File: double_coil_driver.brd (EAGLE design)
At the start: 50 x 50 mm, 62 parts, among them Q1 MOSFET-N, Q3 IRF7493, U1 MCP6L01UT-E/OT, U2 V_REG_LDOSMD, U3 LT3750EMSPBF, X2 MICROMATCH-10

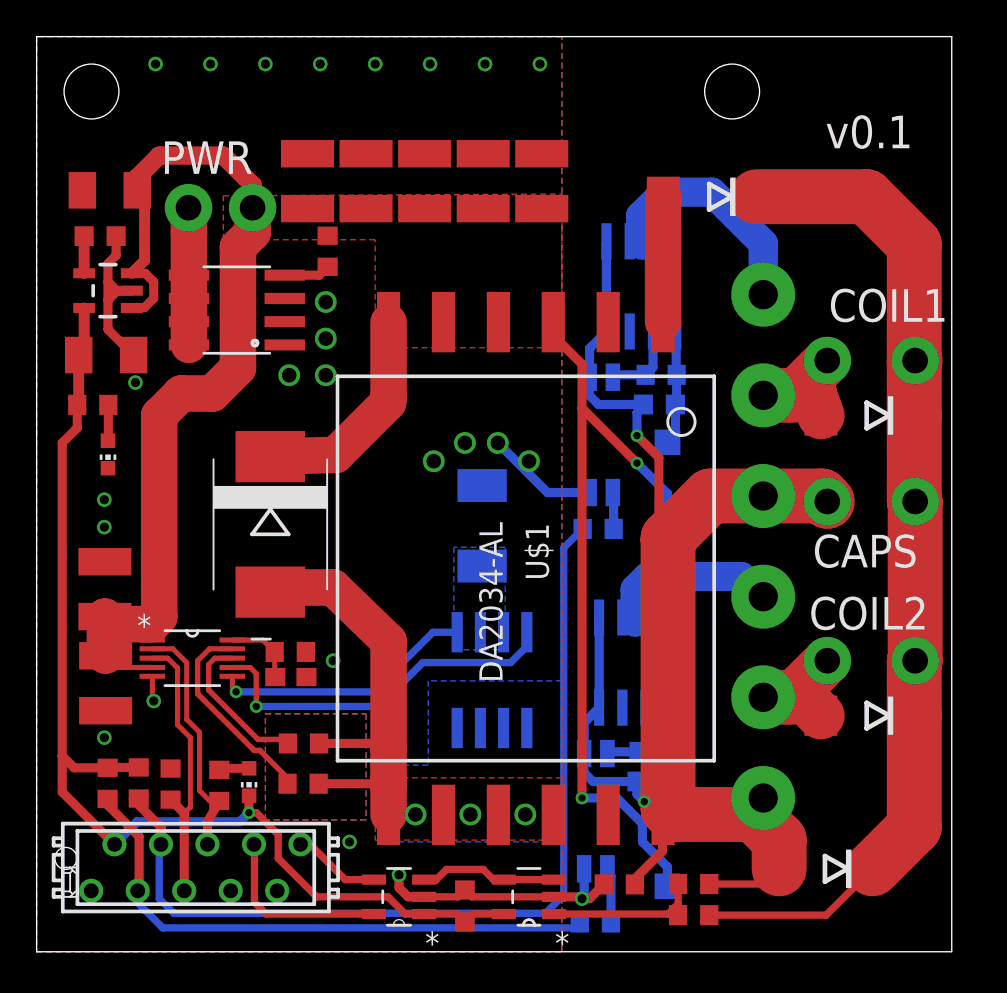
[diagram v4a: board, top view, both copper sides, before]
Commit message: Changed kick pull-ups to pull-downs
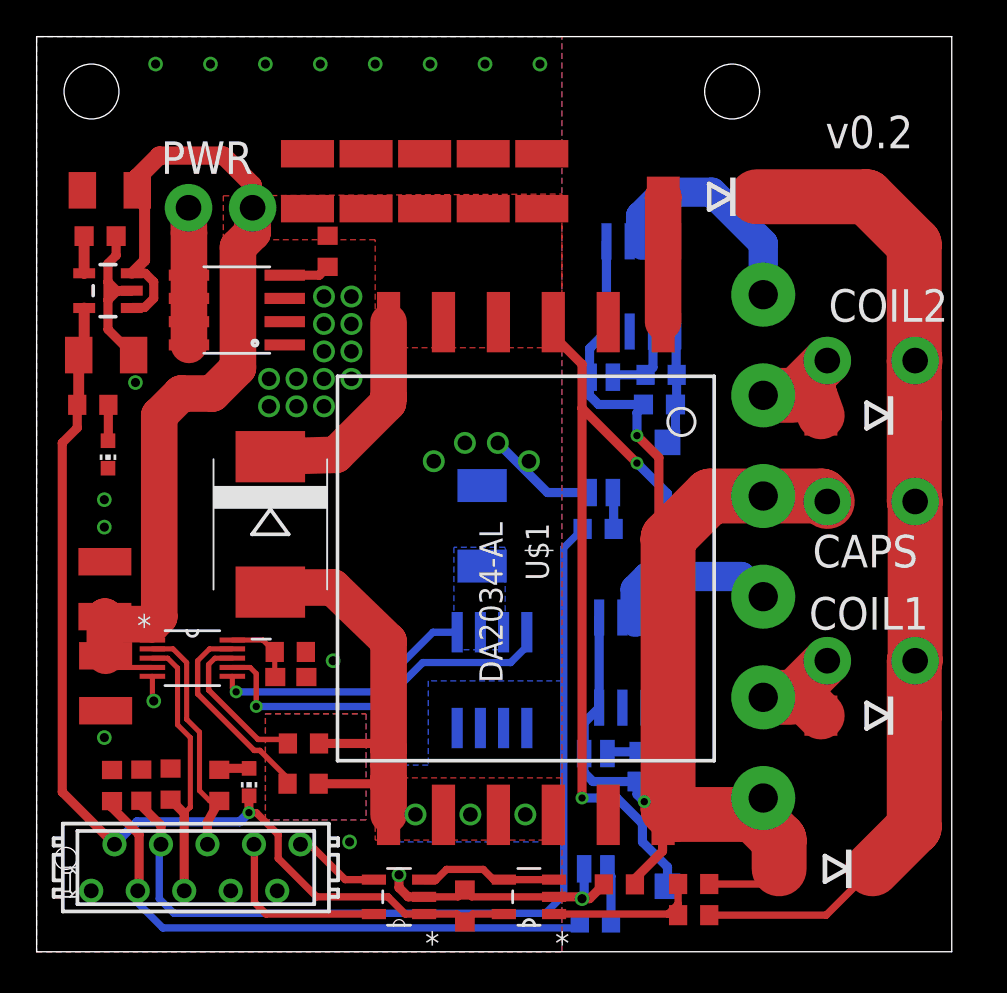
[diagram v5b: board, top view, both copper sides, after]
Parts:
- moved R15 1.84 mm to (5.72, 9.10), turned to 270 degrees
- moved R16 1.47 mm to (4.12, 9.08), turned to 270 degrees
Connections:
- net +5V: no longer R15.2, R16.2
- net GNDA: now also R15.1, R16.1
- net KICK1: now also R16.2; no longer R15.1
- net KICK2: now also R15.2; no longer R16.1
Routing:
- net +5V: track 61.9 -> 57.5 mm
- net KICK2: track 49.7 -> 49.1 mm
- net GNDA: vias 25 -> 34
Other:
- board text added: "v0.2"
- board text removed: "v0.1"
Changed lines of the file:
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@@
 <?xml version="1.0" encoding="utf-8"?>
 <!DOCTYPE eagle SYSTEM "eagle.dtd">
-<eagle version="6.5.0">
+<eagle version="7.0.0">
 <drawing>
 <settings>
@@
 <hole x="3" y="47" drill="3"/>
 <hole x="38" y="47" drill="3"/>
-<text x="49.8" y="36.2" size="1.778" layer="25" rot="R180">COIL1</text>
+<text x="49.8" y="36.2" size="1.778" layer="25" rot="R180">COIL2</text>
 <text x="42.4" y="21" size="1.778" layer="25">CAPS</text>
-<text x="42.2" y="17.6" size="1.778" layer="25">COIL2</text>
+<text x="42.2" y="17.6" size="1.778" layer="25">COIL1</text>
 <text x="6.8" y="42.5" size="1.778" layer="25">PWR</text>
-<text x="43.1" y="43.9" size="1.778" layer="25">v0.1</text>
+<text x="43.1" y="43.9" size="1.778" layer="25">v0.2</text>
 <hole x="1.6" y="5.1" drill="1.2"/>
 </plain>
@@
 <pass name="Default">
 <param name="RoutingGrid" value="50mil"/>
+<param name="AutoGrid" value="1"/>
+<param name="Efforts" value="0"/>
+<param name="TopRouterVariant" value="1"/>
 <param name="tpViaShape" value="round"/>
 <param name="PrefDir.1" value="|"/>
@@
 <attribute name="VALUE" x="34.83" y="28.25" size="1.016" layer="28" rot="MR0"/>
 </element>
-<element name="R15" library="rcl" package="R0603" value="10k" x="3.88" y="9.2" smashed="yes" rot="R90">
-<attribute name="NAME" x="3.245" y="8.565" size="1.27" layer="27" rot="R90"/>
-<attribute name="VALUE" x="5.785" y="8.565" size="1.27" layer="27" rot="R90"/>
-</element>
-<element name="R16" library="rcl" package="R0603" value="10k" x="5.58" y="9.22" smashed="yes" rot="R90">
-<attribute name="NAME" x="4.945" y="8.585" size="1.27" layer="27" rot="R90"/>
-<attribute name="VALUE" x="7.485" y="8.585" size="1.27" layer="27" rot="R90"/>
+<element name="R15" library="rcl" package="R0603" value="10k" x="5.72" y="9.1" smashed="yes" rot="R270">
+<attribute name="NAME" x="6.355" y="9.735" size="1.27" layer="27" rot="R270"/>
+<attribute name="VALUE" x="3.815" y="9.735" size="1.27" layer="27" rot="R270"/>
+</element>
+<element name="R16" library="rcl" package="R0603" value="10k" x="4.12" y="9.08" smashed="yes" rot="R270">
+<attribute name="NAME" x="4.755" y="9.715" size="1.27" layer="27" rot="R270"/>
+<attribute name="VALUE" x="2.215" y="9.715" size="1.27" layer="27" rot="R270"/>
 </element>
 <element name="R17" library="rcl" package="R0603" value="10k" x="7.32" y="9.16" smashed="yes" rot="R270">
@@
 <wire x1="30.215" y1="25.09" x2="27.91" y2="25.09" width="0.5" layer="16"/>
 <wire x1="27.91" y1="25.09" x2="25.2" y2="27.8" width="0.5" layer="16"/>
-<via x="15.8" y="35.5" extent="1-16" drill="0.8"/>
-<via x="15.8" y="33.5" extent="1-16" drill="0.8"/>
-<via x="15.8" y="31.5" extent="1-16" drill="0.8"/>
-<via x="13.8" y="31.5" extent="1-16" drill="0.8"/>
+<via x="15.7" y="35.8" extent="1-16" drill="0.8"/>
+<via x="15.7" y="34.3" extent="1-16" drill="0.8"/>
+<via x="15.7" y="31.3" extent="1-16" drill="0.8"/>
+<via x="12.7" y="29.8" extent="1-16" drill="0.8"/>
 <via x="21.7" y="26.8" extent="1-16" drill="0.8"/>
 <via x="26.9" y="26.8" extent="1-16" drill="0.8"/>
@@
 <via x="24.5" y="48.5" extent="1-16" drill="0.5"/>
 <via x="27.5" y="48.5" extent="1-16" drill="0.5"/>
+<contactref element="R15" pad="1"/>
+<contactref element="R16" pad="1"/>
+<via x="17.2" y="34.3" extent="1-16" drill="0.8"/>
+<via x="17.2" y="32.8" extent="1-16" drill="0.8"/>
+<via x="17.2" y="31.3" extent="1-16" drill="0.8"/>
+<via x="15.7" y="29.8" extent="1-16" drill="0.8"/>
+<via x="14.2" y="29.8" extent="1-16" drill="0.8"/>
+<via x="15.7" y="32.8" extent="1-16" drill="0.8"/>
+<via x="17.2" y="35.8" extent="1-16" drill="0.8"/>
+<via x="14.2" y="31.3" extent="1-16" drill="0.8"/>
+<via x="12.7" y="31.3" extent="1-16" drill="0.8"/>
 </signal>
 <signal name="N$2">
@@
 <contactref element="LED2" pad="C"/>
 <contactref element="C2" pad="1"/>
-<contactref element="R15" pad="2"/>
-<contactref element="R16" pad="2"/>
 <contactref element="U$8" pad="1"/>
 <wire x1="2.5999" y1="35.17" x2="2.5999" y2="32.8999" width="0.6" layer="1"/>
@@
 <wire x1="2.22" y1="29.88" x2="2.22" y2="28.62" width="0.5" layer="1"/>
 <wire x1="2.22" y1="28.62" x2="1.4" y2="27.8" width="0.5" layer="1"/>
-<wire x1="1.4" y1="27.8" x2="1.4" y2="10.7" width="0.5" layer="1"/>
-<wire x1="2.05" y1="10.05" x2="1.4" y2="10.7" width="0.5" layer="1"/>
+<wire x1="1.4" y1="27.8" x2="1.4" y2="8.725" width="0.5" layer="1"/>
 <wire x1="11.61" y1="8.52" x2="11.6" y2="8.61" width="0.5" layer="1"/>
 <wire x1="11.6" y1="8.61" x2="11.6" y2="7.6" width="0.5" layer="1"/>
@@
 <wire x1="11.6" y1="7.6" x2="11.1" y2="7.1" width="0.5" layer="16"/>
 <wire x1="11.1" y1="7.1" x2="5.485" y2="7.1" width="0.5" layer="16"/>
-<wire x1="2.05" y1="10.05" x2="3.88" y2="10.05" width="0.5" layer="1"/>
-<wire x1="3.88" y1="10.05" x2="3.9" y2="10.07" width="0.5" layer="1"/>
-<wire x1="3.9" y1="10.07" x2="5.58" y2="10.07" width="0.5" layer="1"/>
 <contactref element="U1" pad="5"/>
 <contactref element="C4" pad="1"/>
@@
 <wire x1="25.5284" y1="2.0602" x2="23.8352" y2="2.0602" width="0.4" layer="1"/>
 <wire x1="23.8352" y1="2.0602" x2="23.4" y2="1.625" width="0.4" layer="1"/>
-<wire x1="1.4" y1="10.7" x2="1.4" y2="8.725" width="0.5" layer="1"/>
 <wire x1="1.4" y1="8.725" x2="4.255" y2="5.87" width="0.5" layer="1"/>
 <wire x1="13.2" y1="6.4" x2="12" y2="7.6" width="0.4" layer="1"/>
@@
 <signal name="KICK1">
 <contactref element="R10" pad="2"/>
-<contactref element="R15" pad="1"/>
 <contactref element="X2" pad="3"/>
-<wire x1="3.88" y1="8.35" x2="3.88" y2="8.02" width="0.5" layer="1"/>
-<wire x1="3.88" y1="8.02" x2="5.6" y2="6.3" width="0.5" layer="1"/>
-<wire x1="5.6" y1="6.3" x2="5.6" y2="3.405" width="0.5" layer="1"/>
 <wire x1="5.6" y1="3.405" x2="5.525" y2="3.33" width="0.5" layer="1"/>
 <wire x1="5.525" y1="3.175" x2="5.525" y2="3.33" width="0.3" layer="1"/>
@@
 <wire x1="5.5" y1="2.7" x2="5.5" y2="3.305" width="0.4" layer="16"/>
 <wire x1="5.5" y1="3.305" x2="5.525" y2="3.33" width="0.4" layer="16"/>
+<contactref element="R16" pad="2"/>
+<wire x1="5.6" y1="3.405" x2="5.6" y2="6.4" width="0.5" layer="1"/>
+<wire x1="5.6" y1="6.4" x2="4.1" y2="7.9" width="0.5" layer="1"/>
+<wire x1="4.1" y1="7.9" x2="4.1" y2="8.21" width="0.5" layer="1"/>
+<wire x1="4.1" y1="8.21" x2="4.12" y2="8.23" width="0.5" layer="1"/>
 </signal>
 <signal name="KICK2">
 <contactref element="R13" pad="2"/>
-<contactref element="R16" pad="1"/>
 <contactref element="X2" pad="4"/>
-<wire x1="5.58" y1="8.37" x2="5.28" y2="8.32" width="0.5" layer="1"/>
-<wire x1="5.28" y1="8.32" x2="6.8" y2="6.8" width="0.5" layer="1"/>
-<wire x1="6.8" y1="6.8" x2="6.8" y2="5.875" width="0.5" layer="1"/>
 <wire x1="6.8" y1="5.875" x2="6.795" y2="5.87" width="0.5" layer="1"/>
 <wire x1="29.83" y1="23.1" x2="28.8" y2="22.07" width="0.4" layer="16"/>
@@
 <wire x1="6.7" y1="2.9" x2="6.7" y2="5.775" width="0.4" layer="16"/>
 <wire x1="6.7" y1="5.775" x2="6.795" y2="5.87" width="0.4" layer="16"/>
+<contactref element="R15" pad="2"/>
+<wire x1="6.8" y1="5.875" x2="6.8" y2="6.9" width="0.5" layer="1"/>
+<wire x1="6.8" y1="6.9" x2="5.7" y2="8" width="0.5" layer="1"/>
+<wire x1="5.7" y1="8" x2="5.7" y2="8.23" width="0.5" layer="1"/>
+<wire x1="5.7" y1="8.23" x2="5.72" y2="8.25" width="0.5" layer="1"/>
 </signal>
 <signal name="CHARGE">
